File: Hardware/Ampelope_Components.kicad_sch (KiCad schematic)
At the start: 117 parts, among them J1 Conn_01x12_Male, J2 Conn_01x12_Male, J3 Conn_01x12_Male, J4 Conn_01x12_Male, J5 Eurorack_16_pin_power, J6 Conn_01x02_Male, J7 SWD_Header, J8 USB_B_Micro, J9 Conn_01x02_Male, Q1 MMBT3906, Q2 MMBT3906, Q3 MMBT3906, Q4 MMBT3906, Q5 MMBT3906, U1 STM32G431RB, U2 AS3364, U3 LM1117-3.3, U4 TL074, U5 TL074, U6 TL074, Y1 8MHz 20pF

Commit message: Various schematic and PCB tidying
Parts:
- added R57, R58, R59, R60: 1k, Resistor_SMD:R_0603_1608Metric_Pad0.98x0.95mm_HandSolder, symbol Device:R
- Y1: footprint Crystal:Crystal_SMD_5032-2Pin_5.0x3.2mm_HandSoldering -> Crystal:Crystal_SMD_0603-2Pin_6.0x3.5mm
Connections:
- net Env1_Out: now also R57.2; no longer R43.1, R47.1, U6.1
- net Env2_Out: now also R58.2; no longer R44.1, R50.1, U6.7
- net Env3_Out: now also R59.2; no longer R45.1, R51.1, U6.8
- net Env4_Out: now also R60.2; no longer R46.1, R52.1, U6.14
- new net: R43.1, R47.1, R57.1, U6.1
- new net: R44.1, R50.1, R58.1, U6.7
- new net: R46.1, R52.1, R60.1, U6.14
- new net: R45.1, R51.1, R59.1, U6.8
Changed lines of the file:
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@@
-(kicad_sch (version 20210615) (generator eeschema)
+(kicad_sch (version 20210621) (generator eeschema)
   (paper "A3")
   (title_block
@@
     (stroke (width 0) (type solid) (color 0 0 0 0))
   )
-  (wire (pts (xy 187.96 167.64) (xy 198.12 167.64))
+  (wire (pts (xy 187.96 167.64) (xy 189.23 167.64))
     (stroke (width 0) (type solid) (color 0 0 0 0))
   )
@@
     (stroke (width 0) (type solid) (color 0 0 0 0))
   )
-  (wire (pts (xy 187.96 198.12) (xy 198.12 198.12))
+  (wire (pts (xy 187.96 198.12) (xy 189.23 198.12))
     (stroke (width 0) (type solid) (color 0 0 0 0))
   )
@@
     (stroke (width 0) (type solid) (color 0 0 0 0))
   )
-  (wire (pts (xy 187.96 228.6) (xy 198.12 228.6))
+  (wire (pts (xy 187.96 228.6) (xy 189.23 228.6))
     (stroke (width 0) (type solid) (color 0 0 0 0))
   )
@@
     (stroke (width 0) (type solid) (color 0 0 0 0))
   )
-  (wire (pts (xy 187.96 259.08) (xy 198.12 259.08))
+  (wire (pts (xy 187.96 259.08) (xy 189.23 259.08))
     (stroke (width 0) (type solid) (color 0 0 0 0))
   )
@@
     (stroke (width 0) (type solid) (color 0 0 0 0))
   )
+  (wire (pts (xy 196.85 167.64) (xy 198.12 167.64))
+    (stroke (width 0) (type solid) (color 0 0 0 0))
+  )
   (wire (pts (xy 196.85 193.04) (xy 198.12 193.04))
     (stroke (width 0) (type solid) (color 0 0 0 0))
   )
+  (wire (pts (xy 196.85 198.12) (xy 198.12 198.12))
+    (stroke (width 0) (type solid) (color 0 0 0 0))
+  )
   (wire (pts (xy 196.85 223.52) (xy 198.12 223.52))
     (stroke (width 0) (type solid) (color 0 0 0 0))
   )
+  (wire (pts (xy 196.85 228.6) (xy 198.12 228.6))
+    (stroke (width 0) (type solid) (color 0 0 0 0))
+  )
   (wire (pts (xy 196.85 254) (xy 198.12 254))
     (stroke (width 0) (type solid) (color 0 0 0 0))
   )
+  (wire (pts (xy 196.85 259.08) (xy 198.12 259.08))
+    (stroke (width 0) (type solid) (color 0 0 0 0))
+  )
   (wire (pts (xy 231.14 168.91) (xy 234.95 168.91))
     (stroke (width 0) (type solid) (color 0 0 0 0))
@@
     (pin "2")
   )
+  (symbol (lib_id "Device:R") (at 193.04 167.64 90) (unit 1)
+    (in_bom yes) (on_board yes)
+    (property "Reference" "R57" (id 0) (at 193.04 170.18 90))
+    (property "Value" "1k" (id 1) (at 193.04 167.64 90))
+    (property "Footprint" "Resistor_SMD:R_0603_1608Metric_Pad0.98x0.95mm_HandSolder" (id 2) (at 193.04 169.418 90)
+      (effects (font (size 1.27 1.27)) hide)
+    )
+    (property "Datasheet" "~" (id 3) (at 193.04 167.64 0)
+      (effects (font (size 1.27 1.27)) hide)
+    )
+    (property "Part_Number" "C25819" (id 4) (at 193.04 167.64 0)
+      (effects (font (size 1.27 1.27)) hide)
+    )
+    (pin "1")
+    (pin "2")
+  )
   (symbol (lib_id "Device:R") (at 193.04 193.04 90) (unit 1)
     (in_bom yes) (on_board yes)
@@
     (pin "2")
   )
+  (symbol (lib_id "Device:R") (at 193.04 198.12 90) (unit 1)
+    (in_bom yes) (on_board yes)
+    (property "Reference" "R58" (id 0) (at 193.04 200.66 90))
+    (property "Value" "1k" (id 1) (at 193.04 198.12 90))
+    (property "Footprint" "Resistor_SMD:R_0603_1608Metric_Pad0.98x0.95mm_HandSolder" (id 2) (at 193.04 199.898 90)
+      (effects (font (size 1.27 1.27)) hide)
+    )
+    (property "Datasheet" "~" (id 3) (at 193.04 198.12 0)
+      (effects (font (size 1.27 1.27)) hide)
+    )
+    (property "Part_Number" "C25819" (id 4) (at 193.04 198.12 0)
+      (effects (font (size 1.27 1.27)) hide)
+    )
+    (pin "1")
+    (pin "2")
+  )
   (symbol (lib_id "Device:R") (at 193.04 223.52 90) (unit 1)
     (in_bom yes) (on_board yes)
@@
     (pin "2")
   )
+  (symbol (lib_id "Device:R") (at 193.04 228.6 90) (unit 1)
+    (in_bom yes) (on_board yes)
+    (property "Reference" "R59" (id 0) (at 193.04 231.14 90))
+    (property "Value" "1k" (id 1) (at 193.04 228.6 90))
+    (property "Footprint" "Resistor_SMD:R_0603_1608Metric_Pad0.98x0.95mm_HandSolder" (id 2) (at 193.04 230.378 90)
+      (effects (font (size 1.27 1.27)) hide)
+    )
+    (property "Datasheet" "~" (id 3) (at 193.04 228.6 0)
+      (effects (font (size 1.27 1.27)) hide)
+    )
+    (property "Part_Number" "C25819" (id 4) (at 193.04 228.6 0)
+      (effects (font (size 1.27 1.27)) hide)
+    )
+    (pin "1")
+    (pin "2")
+  )
   (symbol (lib_id "Device:R") (at 193.04 254 90) (unit 1)
     (in_bom yes) (on_board yes)
@@
     (pin "2")
   )
+  (symbol (lib_id "Device:R") (at 193.04 259.08 90) (unit 1)
+    (in_bom yes) (on_board yes)
+    (property "Reference" "R60" (id 0) (at 193.04 261.62 90))
+    (property "Value" "1k" (id 1) (at 193.04 259.08 90))
+    (property "Footprint" "Resistor_SMD:R_0603_1608Metric_Pad0.98x0.95mm_HandSolder" (id 2) (at 193.04 260.858 90)
+      (effects (font (size 1.27 1.27)) hide)
+    )
+    (property "Datasheet" "~" (id 3) (at 193.04 259.08 0)
+      (effects (font (size 1.27 1.27)) hide)
+    )
+    (property "Part_Number" "C25819" (id 4) (at 193.04 259.08 0)
+      (effects (font (size 1.27 1.27)) hide)
+    )
+    (pin "1")
+    (pin "2")
+  )
   (symbol (lib_id "Device:C_Small") (at 20.32 62.23 180) (unit 1)
     (in_bom yes) (on_board yes)
@@
       (effects (font (size 1.27 1.27)) (justify right))
     )
-    (property "Footprint" "Crystal:Crystal_SMD_5032-2Pin_5.0x3.2mm_HandSoldering" (id 2) (at 44.45 71.12 0)
+    (property "Footprint" "Crystal:Crystal_SMD_0603-2Pin_6.0x3.5mm" (id 2) (at 44.45 71.12 0)
       (effects (font (size 1.27 1.27)) hide)
     )
@@
       (effects (font (size 1.27 1.27) italic) (justify left) hide)
     )
-    (property "Datasheet" "https://www.onsemi.com/pub/Collateral/2N3906-D.PDF" (id 3) (at 323.85 160.02 0)
+    (property "Datasheet" "https://www.mouser.co.uk/datasheet/2/115/DIOD_S_A0012992517_1-2513078.pdf" (id 3) (at 323.85 160.02 0)
       (effects (font (size 1.27 1.27)) (justify left) hide)
     )
@@
       (effects (font (size 1.27 1.27) italic) (justify left) hide)
     )
-    (property "Datasheet" "https://www.onsemi.com/pub/Collateral/2N3906-D.PDF" (id 3) (at 323.85 191.77 0)
+    (property "Datasheet" "https://www.mouser.co.uk/datasheet/2/115/DIOD_S_A0012992517_1-2513078.pdf" (id 3) (at 323.85 191.77 0)
       (effects (font (size 1.27 1.27)) (justify left) hide)
     )
@@
       (effects (font (size 1.27 1.27) italic) (justify left) hide)
     )
-    (property "Datasheet" "https://www.onsemi.com/pub/Collateral/2N3906-D.PDF" (id 3) (at 323.85 223.52 0)
+    (property "Datasheet" "https://www.mouser.co.uk/datasheet/2/115/DIOD_S_A0012992517_1-2513078.pdf" (id 3) (at 323.85 223.52 0)
       (effects (font (size 1.27 1.27)) (justify left) hide)
     )
@@
       (effects (font (size 1.27 1.27) italic) (justify left) hide)
     )
-    (property "Datasheet" "https://www.onsemi.com/pub/Collateral/2N3906-D.PDF" (id 3) (at 377.19 160.02 0)
+    (property "Datasheet" "https://www.mouser.co.uk/datasheet/2/115/DIOD_S_A0012992517_1-2513078.pdf" (id 3) (at 377.19 160.02 0)
       (effects (font (size 1.27 1.27)) (justify left) hide)
     )
@@
       (effects (font (size 1.27 1.27) italic) (justify left) hide)
     )
-    (property "Datasheet" "https://www.onsemi.com/pub/Collateral/2N3906-D.PDF" (id 3) (at 377.19 191.77 0)
+    (property "Datasheet" "https://www.mouser.co.uk/datasheet/2/115/DIOD_S_A0012992517_1-2513078.pdf" (id 3) (at 377.19 191.77 0)
       (effects (font (size 1.27 1.27)) (justify left) hide)
     )
@@
       (reference "R56") (unit 1) (value "10k") (footprint "Resistor_SMD:R_0603_1608Metric_Pad0.98x0.95mm_HandSolder")
     )
+    (path "/0ad8054e-920a-4247-a0df-114da6306e0c"
+      (reference "R57") (unit 1) (value "1k") (footprint "Resistor_SMD:R_0603_1608Metric_Pad0.98x0.95mm_HandSolder")
+    )
+    (path "/c9b3c985-c75b-41c4-8689-b35f1e90c4a8"
+      (reference "R58") (unit 1) (value "1k") (footprint "Resistor_SMD:R_0603_1608Metric_Pad0.98x0.95mm_HandSolder")
+    )
+    (path "/bb9d1e66-c71a-4b7e-a761-b69b86a7bc3b"
+      (reference "R59") (unit 1) (value "1k") (footprint "Resistor_SMD:R_0603_1608Metric_Pad0.98x0.95mm_HandSolder")
+    )
+    (path "/fd10a731-ad3a-47e1-adbb-104b97e114b0"
+      (reference "R60") (unit 1) (value "1k") (footprint "Resistor_SMD:R_0603_1608Metric_Pad0.98x0.95mm_HandSolder")
+    )
     (path "/7615093a-318c-4c05-a9b3-abeff2838590"
       (reference "RESET1") (unit 1) (value "SW_Push") (footprint "Custom_Footprints:SW_SPST_EVQQ2")
@@
     )
     (path "/1017b0fa-b29a-4df9-90e1-b97f4fe34130"
-      (reference "Y1") (unit 1) (value "8MHz 20pF") (footprint "Crystal:Crystal_SMD_5032-2Pin_5.0x3.2mm_HandSoldering")
+      (reference "Y1") (unit 1) (value "8MHz 20pF") (footprint "Crystal:Crystal_SMD_0603-2Pin_6.0x3.5mm")
     )
   )

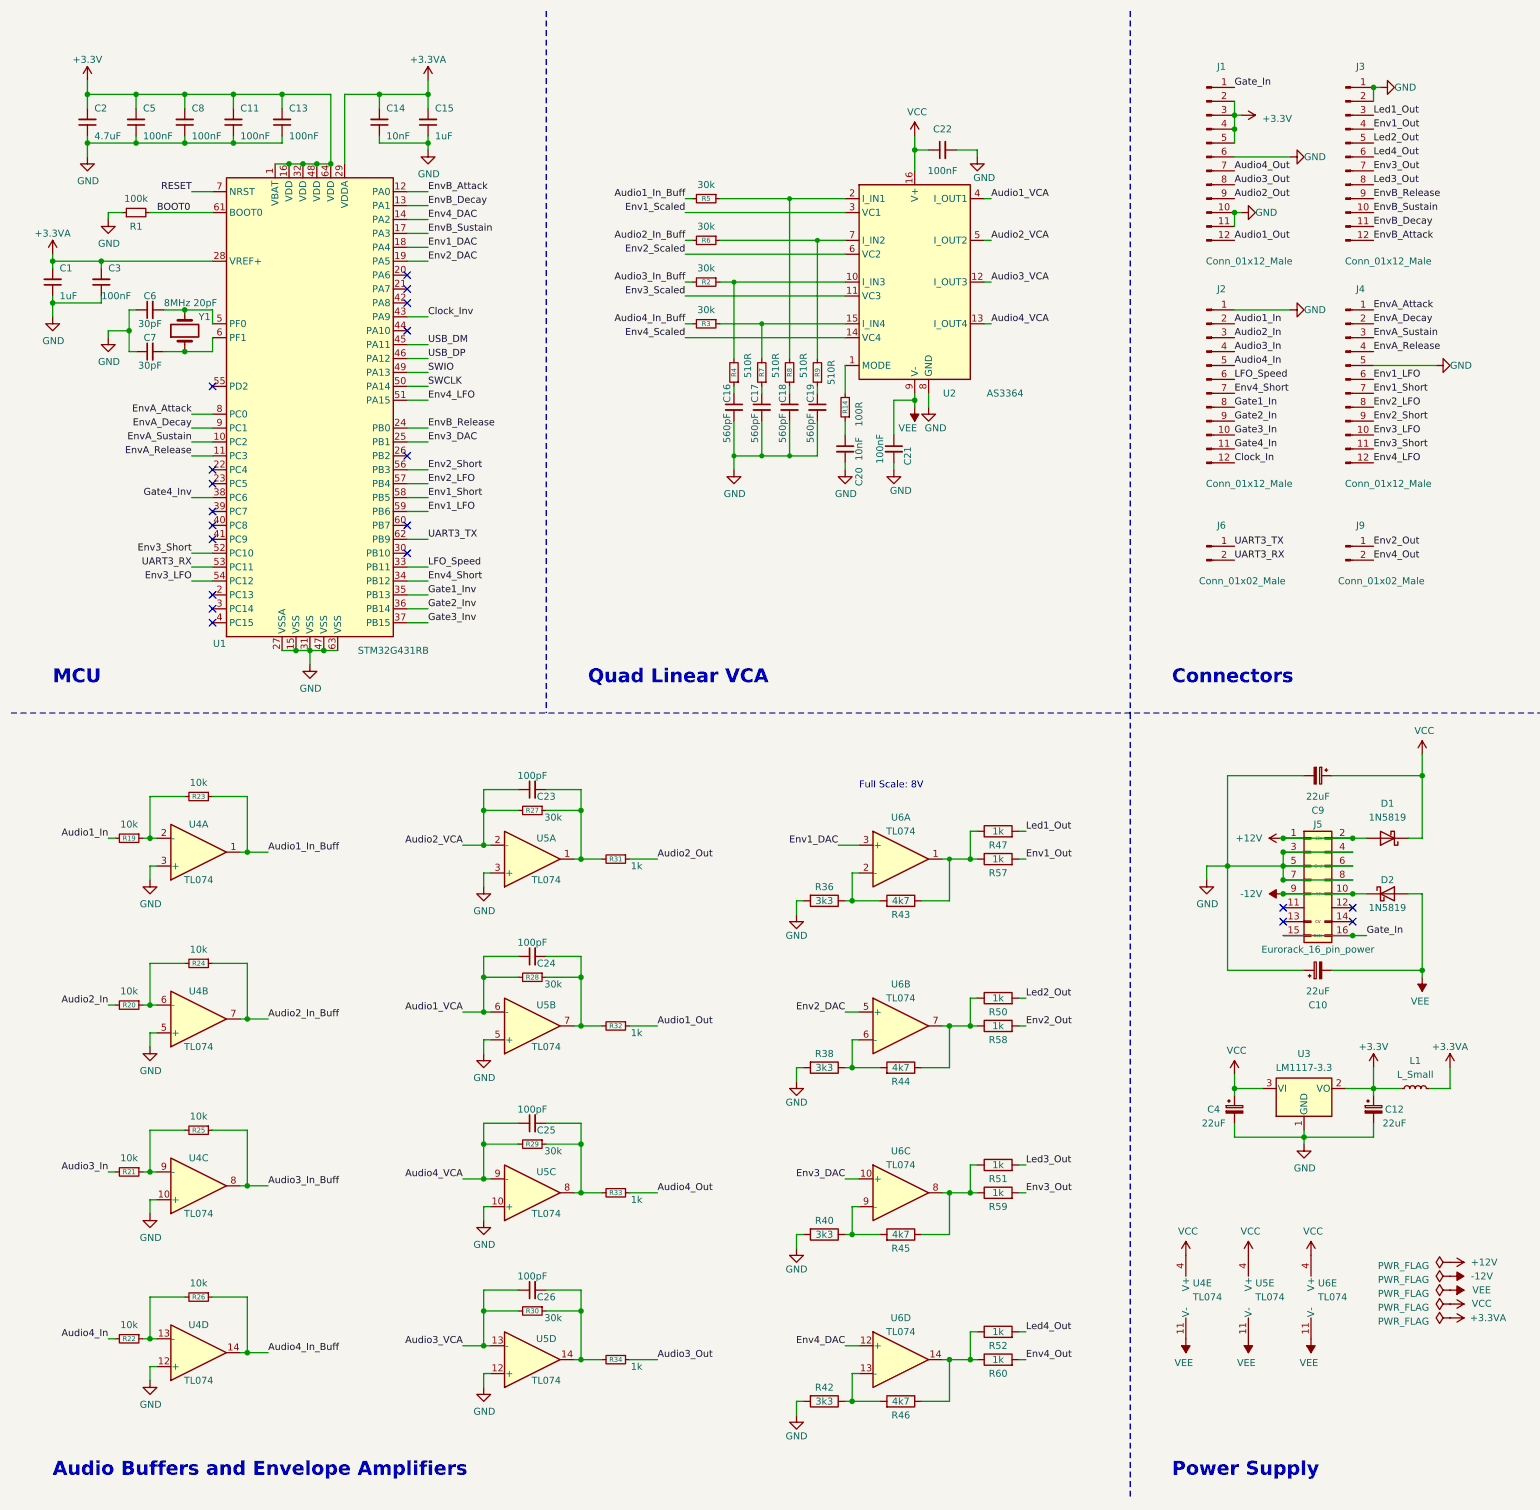
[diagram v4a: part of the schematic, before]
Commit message: Further PCB tidy up and DAC testing
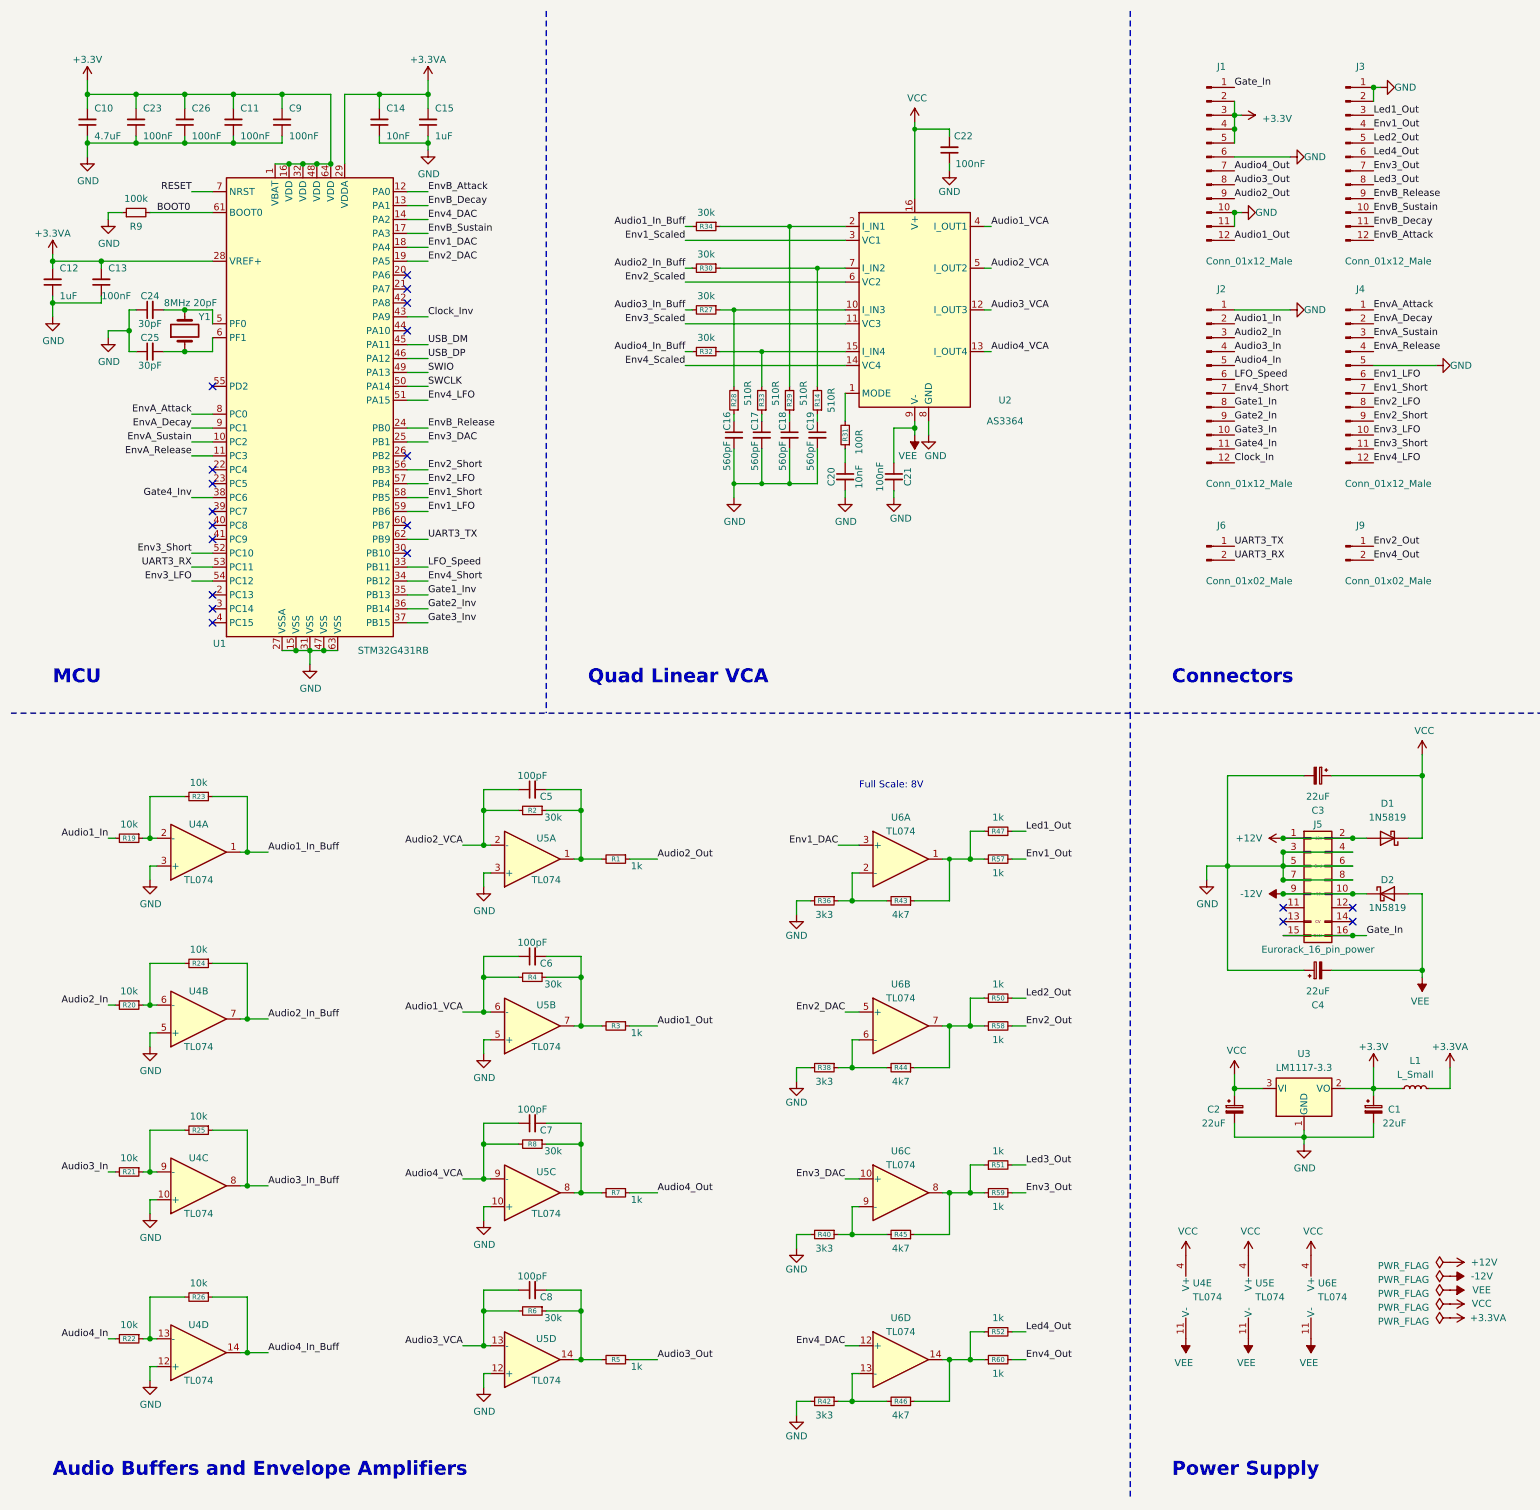
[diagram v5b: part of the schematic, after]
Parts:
- R36, R38, R40, R42, R43, R44, R45, R46, R47, R50, R51, R52, R57, R58, R59, R60: symbol Device:R -> Device:R_Small
- renumbered C12 to C1, C2 to C10, C1 to C12, C3 to C13, C4 to C2, C5 to C23, C6 to C24, C7 to C25, C8 to C26, C9 to C3, C10 to C4, C23 to C5, C24 to C6, C25 to C7, C26 to C8, C13 to C9, R31 to R1, R9 to R14, R27 to R2, R2 to R27, R4 to R28, R8 to R29, R32 to R3, R6 to R30, R14 to R31, R3 to R32, R7 to R33, R5 to R34, R28 to R4, R34 to R5, R30 to R6, R33 to R7, R29 to R8, R1 to R9
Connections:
- net GND: now also C22.1; no longer C22.2
- net VCC: now also C22.2; no longer C22.1
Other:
- moved on the sheet: C16, C17, C18, C19, C20, C21, C22, R14, R27, R28, R29, R30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
